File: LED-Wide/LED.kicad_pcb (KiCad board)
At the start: 2 copper layers, 20.4 x 10.4 mm, 4 parts

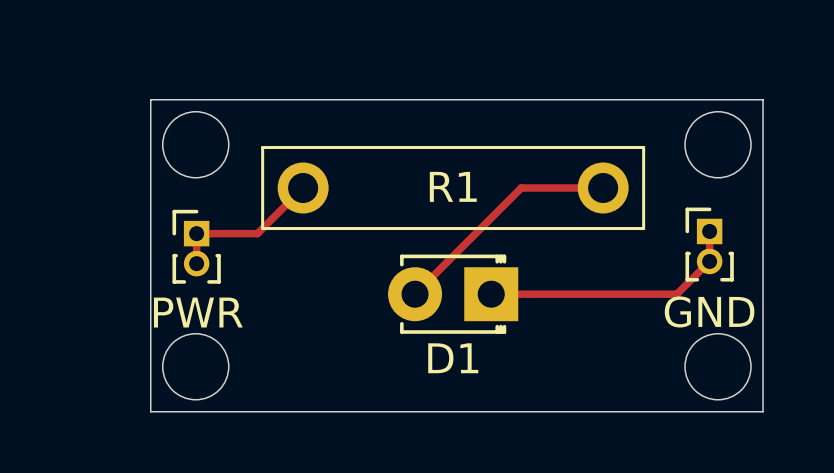
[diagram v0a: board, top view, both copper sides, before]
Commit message: Box design and LED PCB alignment changes
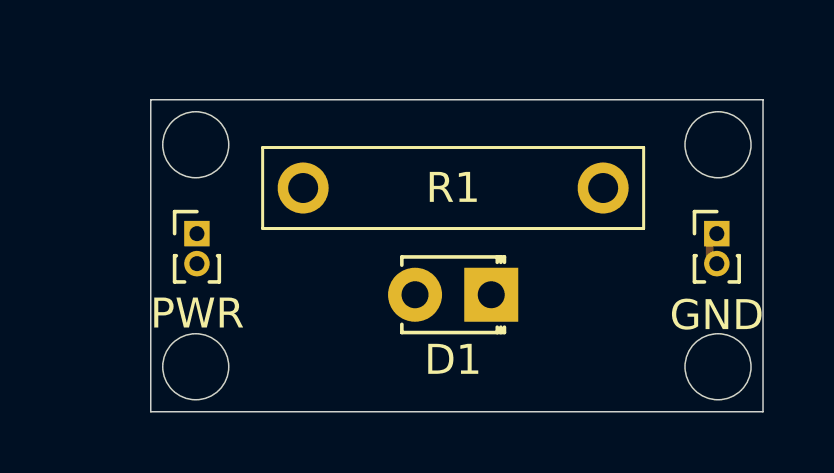
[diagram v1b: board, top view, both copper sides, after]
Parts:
- moved GND 0.25 mm to (159.9, 85.8)
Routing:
- net Net-(D1-A): track 7.74 -> 0.00 mm
- net GND: track 8.73 -> 1.00 mm
- net PWR: track 5.18 -> 0.00 mm
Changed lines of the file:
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@@
 	(footprint "LED_THT:LED_D1.8mm_W3.3mm_H2.4mm"
 		(layer "F.Cu")
-		(at 152.35 87.782 180)
+		(at 152.35 87.8 180)
 		(descr "LED, Round, Rectangular, size 3.3x2.4mm, diameter 1.8mm, 2 pins, generated by kicad-footprint-generator")
 		(tags "LED")
@@
 	(footprint "Connector_PinHeader_1.00mm:PinHeader_1x02_P1.00mm_Vertical"
 		(layer "F.Cu")
-		(at 142.53 85.763333)
+		(at 142.54 85.763333)
 		(descr "Through hole straight pin header, 1x02, 1.00mm pitch, single row")
 		(tags "Through hole pin header THT 1x02 1.00mm single row")
@@
 	(footprint "Connector_PinHeader_1.00mm:PinHeader_1x02_P1.00mm_Vertical"
 		(layer "F.Cu")
-		(at 159.63 85.69)
+		(at 159.869 85.763)
 		(descr "Through hole straight pin header, 1x02, 1.00mm pitch, single row")
 		(tags "Through hole pin header THT 1x02 1.00mm single row")
@@
 	)
 	(segment
-		(start 158.538 87.782)
-		(end 159.63 86.69)
-		(width 0.25)
-		(layer "F.Cu")
-		(net 1)
-	)
-	(segment
-		(start 152.35 87.782)
-		(end 158.538 87.782)
-		(width 0.25)
-		(layer "F.Cu")
-		(net 1)
-	)
-	(segment
 		(start 159.63 86.69)
 		(end 159.63 85.69)
@@
 		(net 1)
 	)
-	(segment
-		(start 153.35 84.242)
-		(end 149.81 87.782)
-		(width 0.25)
-		(layer "F.Cu")
-		(net 2)
-	)
-	(segment
-		(start 156.08 84.242)
-		(end 153.35 84.242)
-		(width 0.25)
-		(layer "F.Cu")
-		(net 2)
-	)
-	(segment
-		(start 142.53 85.763333)
-		(end 144.558667 85.763333)
-		(width 0.25)
-		(layer "F.Cu")
-		(net 3)
-	)
-	(segment
-		(start 142.53 86.763333)
-		(end 142.53 85.763333)
-		(width 0.25)
-		(layer "F.Cu")
-		(net 3)
-	)
-	(segment
-		(start 144.558667 85.763333)
-		(end 146.08 84.242)
-		(width 0.25)
-		(layer "F.Cu")
-		(net 3)
-	)
 	(embedded_fonts no)

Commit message: added tracks to LED-Wide PCB
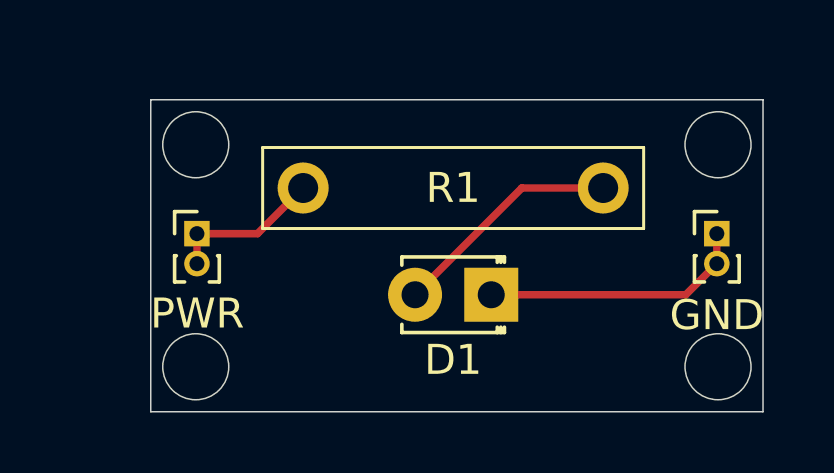
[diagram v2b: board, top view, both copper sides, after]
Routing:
- net GND: track 1.00 -> 8.95 mm
- net Net-(D1-A): track 0.00 -> 7.74 mm
- net PWR: track 0.00 -> 5.17 mm
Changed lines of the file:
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@@
 	)
 	(segment
-		(start 159.63 86.69)
-		(end 159.63 85.69)
+		(start 158.832 87.8)
+		(end 159.869 86.763)
 		(width 0.25)
 		(layer "F.Cu")
 		(net 1)
 	)
+	(segment
+		(start 159.869 86.763)
+		(end 159.869 85.763)
+		(width 0.25)
+		(layer "F.Cu")
+		(net 1)
+	)
+	(segment
+		(start 152.35 87.8)
+		(end 158.832 87.8)
+		(width 0.25)
+		(layer "F.Cu")
+		(net 1)
+	)
+	(segment
+		(start 153.368 84.242)
+		(end 149.81 87.8)
+		(width 0.25)
+		(layer "F.Cu")
+		(net 2)
+	)
+	(segment
+		(start 156.08 84.242)
+		(end 153.368 84.242)
+		(width 0.25)
+		(layer "F.Cu")
+		(net 2)
+	)
+	(segment
+		(start 144.558667 85.763333)
+		(end 146.08 84.242)
+		(width 0.25)
+		(layer "F.Cu")
+		(net 3)
+	)
+	(segment
+		(start 142.54 85.763333)
+		(end 144.558667 85.763333)
+		(width 0.25)
+		(layer "F.Cu")
+		(net 3)
+	)
+	(segment
+		(start 142.54 86.763333)
+		(end 142.54 85.763333)
+		(width 0.25)
+		(layer "F.Cu")
+		(net 3)
+	)
 	(embedded_fonts no)

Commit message: Redesigned LED-Wide PCB; created Fabrication files; added template for fabrication order request; added final order contents.
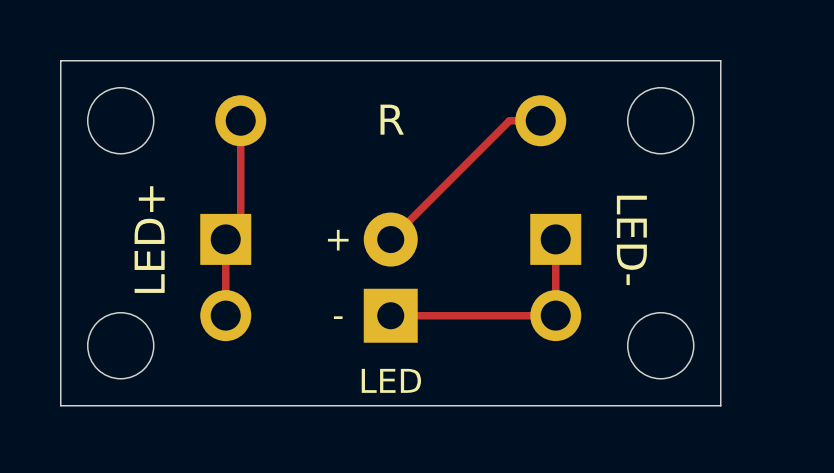
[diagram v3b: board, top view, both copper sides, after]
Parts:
- removed GND, PWR: Conn_01x02_Pin, Connector_PinHeader_1.00mm:PinHeader_1x02_P1.00mm_Vertical
- added LED+: Conn_01x02_Pin, Connector_PinHeader_2.54mm:PinHeader_1x02_P2.54mm_Vertical, F.Cu at (143.5, 86.0)
- added LED-: Conn_01x02_Pin, Connector_PinHeader_2.54mm:PinHeader_1x02_P2.54mm_Vertical, F.Cu at (154.5, 86.0)
- LED: renamed from D1; footprint LED_THT:LED_D1.8mm_W3.3mm_H2.4mm -> LED_THT:LED_D5.0mm
- moved LED 3.42 mm to (149.0, 88.5), turned to 90 degrees
- moved R 3.06 mm to (149.0, 82.0)
- renumbered R1 to R
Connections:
- LED pad 1: GND -> LED-
- R pad 1: PWR -> LED+
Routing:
- net GND: track 8.95 -> 0.00 mm
- net LED-: track 0.00 -> 8.04 mm
- net LED+: track 0.00 -> 6.70 mm
- net PWR: track 5.17 -> 0.00 mm
- net Net-(D1-A): track 7.74 -> 6.64 mm
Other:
- board size 20.4 x 10.4 mm -> 22 x 11.5 mm
- board text added: "+"
- board text added: "-"
